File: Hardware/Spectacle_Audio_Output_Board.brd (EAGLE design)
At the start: 25.4 x 55.9 mm, 77 parts, among them J3 Audio Jack, J4 AUDIO-JACK3, J5 AUDIO-JACK3, U1 CY8C4146LQI-S422, U2 3.3V, U3 3.3V, U4 AT25SF041-SOIC8, Y1 12MHz

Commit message: Submitted for review by QC
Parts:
- added C11: 10uF, SparkFun-Capacitors:0603-CAP
- added FD5, FD6, FD7, FD8: FIDUCIALUFIDUCIAL, SparkFun-Aesthetics:MICRO-FIDUCIAL
- added R2: 1M, SparkFun-Resistors:0603-RES
- J3: value Audio Jack -> (none); device SparkFun-Connectors:STEREOJACK2.5MM_SMD -> SparkFun-Connectors:AUDIO-JACK-3.5MM-SMD
- moved C12 15.6 mm to (13.8, 27.8), turned to 90 degrees
- moved R20 7.80 mm to (19.2, 49.8), turned to 180 degrees
- moved R19 5.87 mm to (16.9, 40.4), turned to 180 degrees
- moved C13 5.08 mm to (19.2, 48.3)
- moved C15 5.08 mm to (19.2, 46.7)
- moved R21 5.08 mm to (22.9, 48.3)
- moved R24 5.08 mm to (22.9, 46.7)
- moved R22 3.07 mm to (20.6, 41.9)
- moved R23 3.07 mm to (20.6, 43.4)
- moved C14 3.07 mm to (16.9, 41.9)
- moved C16 3.07 mm to (16.9, 43.4)
- moved J3 2.54 mm to (0.00, 45.7)
- moved SW2 1.27 mm to (20.3, 34.3)
- moved U4 0.81 mm to (19.6, 29.8)
- moved C19 0.13 mm to (20.7, 18.2)
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- renumbered U$2 to U5
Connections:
- new net VCCIO: C12.1, R11.2, R12.2, R13.2, R14.2, R15.2, R16.2, R17.2, R29.2, U5.19, U5.30, U5.7
- new net VDDA: C11.1, U5.34, U5.39, U5.44, U5.46
- net 3.3V: now also C21.2; no longer C12.1, R11.2, R12.2, R13.2, R14.2, R15.2, R16.2, R17.2, R26.1, R29.2, U5.19, U5.30, U5.34, U5.39, U5.44, U5.46, U5.7
- net GND: now also C11.2, J3.SLEEVE, R2.2, R26.2; no longer C21.1, J3.5
- net L_AC: now also J3.TIP; no longer J3.1
- net N$12: now also R2.1
- net N$15: now also C21.1, R26.1; no longer C21.2, R26.2
- net R_AC: now also J3.RING; no longer J3.4
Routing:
- net VCCIO: track 0.00 -> 92.4 mm, vias 0 -> 10
- net 3.3V: track 65.3 -> 31.0 mm, vias 19 -> 9
- net R_AC: track 4.83 -> 31.6 mm
- net VDDA: track 0.00 -> 17.3 mm
- net L_AC: track 4.83 -> 13.7 mm
- net N$12: track 2.85 -> 11.2 mm, vias 0 -> 2
- net LEFT: track 47.3 -> 52.1 mm
- net VDD: track 23.7 -> 27.4 mm
- net N$7: track 21.6 -> 24.6 mm
- net RIGHT: track 40.7 -> 38.1 mm
- net N$1: track 26.0 -> 28.4 mm
- net SDCK: track 29.4 -> 31.2 mm
- net SCLK: track 8.19 -> 6.74 mm
- net SO: track 9.21 -> 7.92 mm
- net BTN: track 1.90 -> 3.17 mm
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
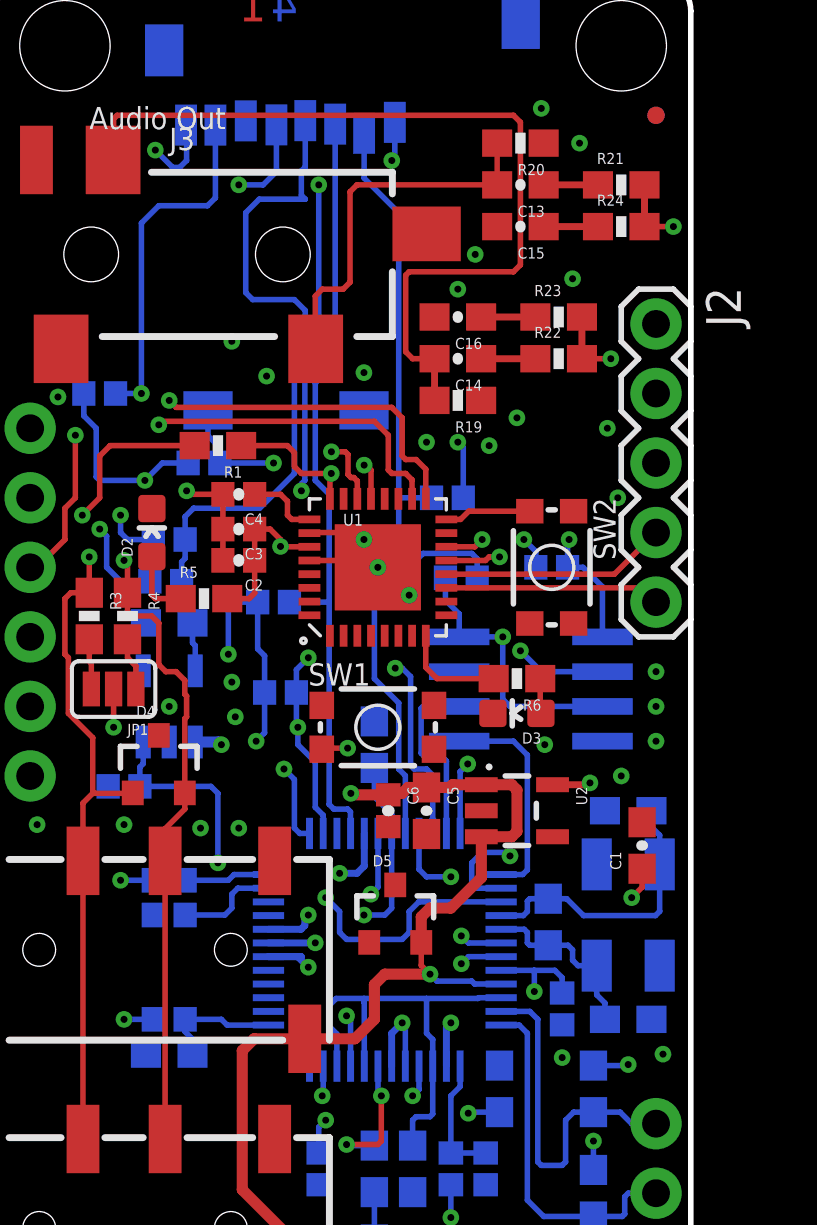
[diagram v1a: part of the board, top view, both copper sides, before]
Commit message: Fixes from QC review
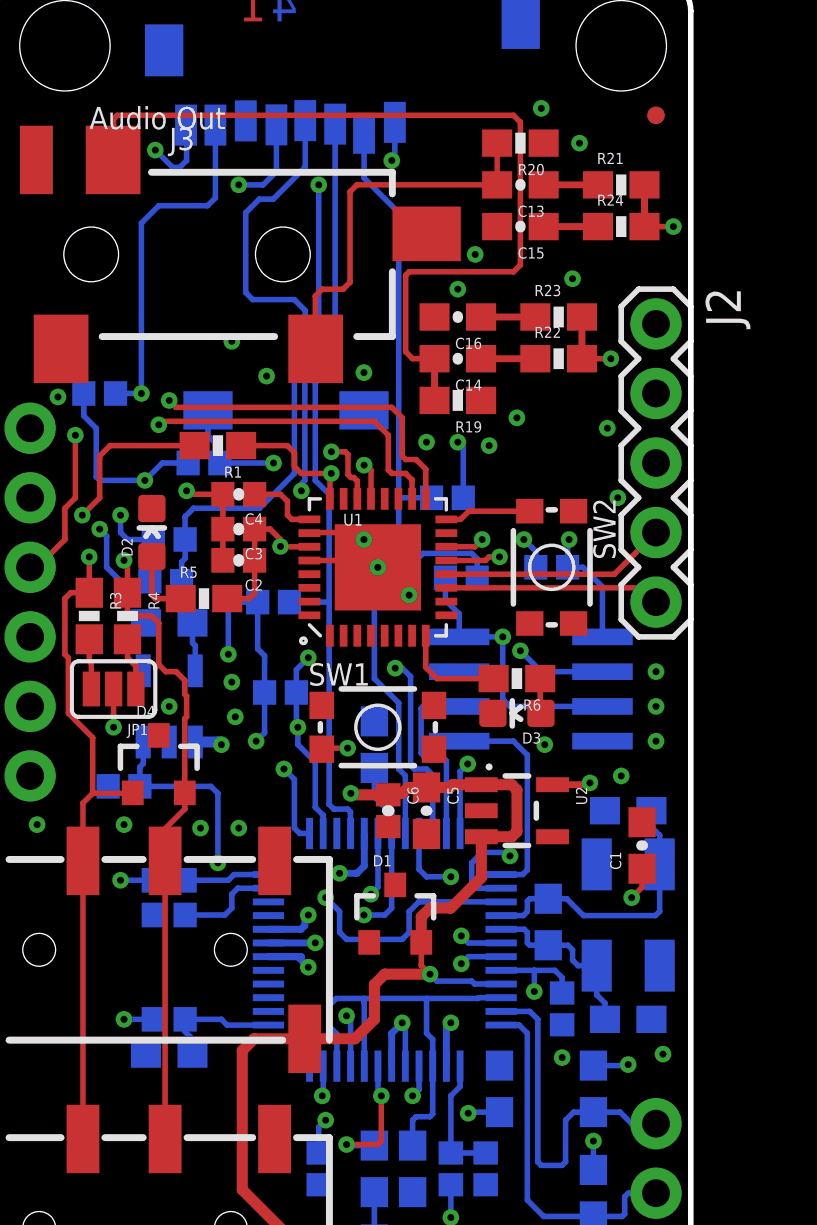
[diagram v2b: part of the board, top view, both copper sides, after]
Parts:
- renumbered C22 to C20, D5 to D1
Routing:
- net N$1: track 28.4 -> 27.0 mm
- net VDD: track 27.4 -> 26.6 mm
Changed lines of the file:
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@@
 <layers>
 <layer number="1" name="Top" color="4" fill="1" visible="no" active="yes"/>
-<layer number="2" name="Route2" color="1" fill="3" visible="no" active="yes"/>
+<layer number="2" name="Route2" color="1" fill="3" visible="yes" active="yes"/>
 <layer number="15" name="Route15" color="4" fill="6" visible="no" active="yes"/>
-<layer number="16" name="Bottom" color="1" fill="1" visible="yes" active="yes"/>
+<layer number="16" name="Bottom" color="1" fill="1" visible="no" active="yes"/>
 <layer number="17" name="Pads" color="2" fill="1" visible="yes" active="yes"/>
 <layer number="18" name="Vias" color="2" fill="1" visible="yes" active="yes"/>
@@
 <layer number="20" name="Dimension" color="15" fill="1" visible="yes" active="yes"/>
 <layer number="21" name="tPlace" color="16" fill="1" visible="no" active="yes"/>
-<layer number="22" name="bPlace" color="14" fill="1" visible="yes" active="yes"/>
+<layer number="22" name="bPlace" color="14" fill="1" visible="no" active="yes"/>
 <layer number="23" name="tOrigins" color="15" fill="1" visible="no" active="yes"/>
-<layer number="24" name="bOrigins" color="15" fill="1" visible="yes" active="yes"/>
+<layer number="24" name="bOrigins" color="15" fill="1" visible="no" active="yes"/>
 <layer number="25" name="tNames" color="7" fill="1" visible="no" active="yes"/>
 <layer number="26" name="bNames" color="7" fill="1" visible="no" active="yes"/>
@@
 <attribute name="PROD_ID" value="DIO-12501" x="5.969" y="27.051" size="1.778" layer="27" font="vector" ratio="15" display="off"/>
 </element>
-<element name="D5" library="SparkFun-DiscreteSemi" package="SOT23-3" value="PESD1CAN" x="14.605" y="21.59">
+<element name="D1" library="SparkFun-DiscreteSemi" package="SOT23-3" value="PESD1CAN" x="14.605" y="21.59">
 <attribute name="PROD_ID" value="DIO-12501" x="14.605" y="21.59" size="1.778" layer="27" font="vector" ratio="15" display="off"/>
 </element>
@@
 <attribute name="PROD_ID" value="RES-13495" x="20.32" y="34.29" size="1.778" layer="28" font="vector" ratio="15" rot="MR0" display="off"/>
 </element>
-<element name="C22" library="SparkFun-Capacitors" package="0603-CAP" value="2.2uF" x="6.35" y="32.258" rot="MR0">
+<element name="C20" library="SparkFun-Capacitors" package="0603-CAP" value="2.2uF" x="6.35" y="32.258" rot="MR0">
 <attribute name="PROD_ID" value="CAP-07888" x="6.35" y="32.258" size="1.778" layer="28" font="vector" ratio="15" rot="MR0" display="off"/>
 </element>
@@
 <contactref element="J4" pad="TIP"/>
 <contactref element="D4" pad="3"/>
-<contactref element="D5" pad="3"/>
+<contactref element="D1" pad="3"/>
 <polygon width="0.2032" layer="1" isolate="0.3048" rank="2">
 <vertex x="0" y="1.27"/>
@@
 <contactref element="U3" pad="2"/>
 <contactref element="U4" pad="4"/>
-<contactref element="C22" pad="2"/>
+<contactref element="C20" pad="2"/>
 <via x="16.637" y="17.653" extent="1-16" drill="0.254"/>
 <via x="14.859" y="17.653" extent="1-16" drill="0.254"/>
@@
 <wire x1="13.974" y1="22.61" x2="13.716" y2="22.352" width="0.2032" layer="16"/>
 <via x="13.716" y="22.352" extent="1-16" drill="0.254"/>
-<wire x1="20.574" y1="16.51" x2="20.701" y2="16.383" width="0.2032" layer="16"/>
 <via x="20.701" y="16.383" extent="1-16" drill="0.254"/>
 <via x="22.86" y="26.67" extent="1-16" drill="0.254"/>
@@
 <contactref element="C5" pad="1"/>
 <contactref element="J4" pad="EARTH"/>
-<contactref element="D5" pad="2"/>
+<contactref element="D1" pad="2"/>
 <contactref element="U3" pad="1"/>
 <contactref element="U5" pad="33"/>
@@
 <contactref element="R7" pad="2"/>
 <contactref element="JP2" pad="4"/>
-<contactref element="C22" pad="1"/>
+<contactref element="C20" pad="1"/>
 <wire x1="7.3" y1="30.5101" x2="7.3" y2="31.435" width="0.2032" layer="16"/>
 <wire x1="7.3" y1="31.435" x2="7.2" y2="31.535" width="0.2032" layer="16"/>
@@
 <wire x1="6.93" y1="34.616" x2="6.93" y2="35.306" width="0.2032" layer="16"/>
 <wire x1="11.318425" y1="50.606296875" x2="11.318425" y2="48.910425" width="0.2032" layer="16"/>
-<wire x1="11.318425" y1="48.910425" x2="11.176" y2="48.768" width="0.2032" layer="16"/>
-<wire x1="11.176" y1="48.768" x2="11.176" y2="47.879" width="0.2032" layer="16"/>
-<wire x1="11.176" y1="47.879" x2="11.318425" y2="47.736575" width="0.2032" layer="16"/>
 <wire x1="11.318425" y1="41.925425" x2="10.922" y2="41.529" width="0.2032" layer="16"/>
 <wire x1="10.922" y1="41.529" x2="10.922" y2="37.719" width="0.2032" layer="16"/>
@@
 <wire x1="9.144" y1="44.323" x2="9.144" y2="47.244" width="0.2032" layer="16"/>
 <wire x1="9.144" y1="47.244" x2="9.636575" y2="47.736575" width="0.2032" layer="16"/>
-<wire x1="9.636575" y1="47.736575" x2="11.318425" y2="47.736575" width="0.2032" layer="16"/>
 <wire x1="11.318425" y1="41.925425" x2="11.318425" y2="43.672575" width="0.2032" layer="16"/>
+<wire x1="9.636575" y1="47.736575" x2="10.144575" y2="47.736575" width="0.2032" layer="16"/>
+<wire x1="10.144575" y1="47.736575" x2="11.318425" y2="48.910425" width="0.2032" layer="16"/>
 </signal>
 <signal name="N$1">
@@
 <wire x1="14.605" y1="50.52741875" x2="14.589215625" y2="50.543203125" width="0.2032" layer="16"/>
 <wire x1="14.097" y1="48.768" x2="14.478" y2="49.149" width="0.2032" layer="2"/>
-<wire x1="14.478" y1="49.149" x2="14.478" y2="50.4319875" width="0.2032" layer="2"/>
-<wire x1="14.478" y1="50.4319875" x2="14.589215625" y2="50.543203125" width="0.2032" layer="2"/>
 <wire x1="14.589215625" y1="50.543203125" x2="14.589215625" y2="49.260215625" width="0.2032" layer="16"/>
 <wire x1="14.589215625" y1="49.260215625" x2="14.478" y2="49.149" width="0.2032" layer="16"/>

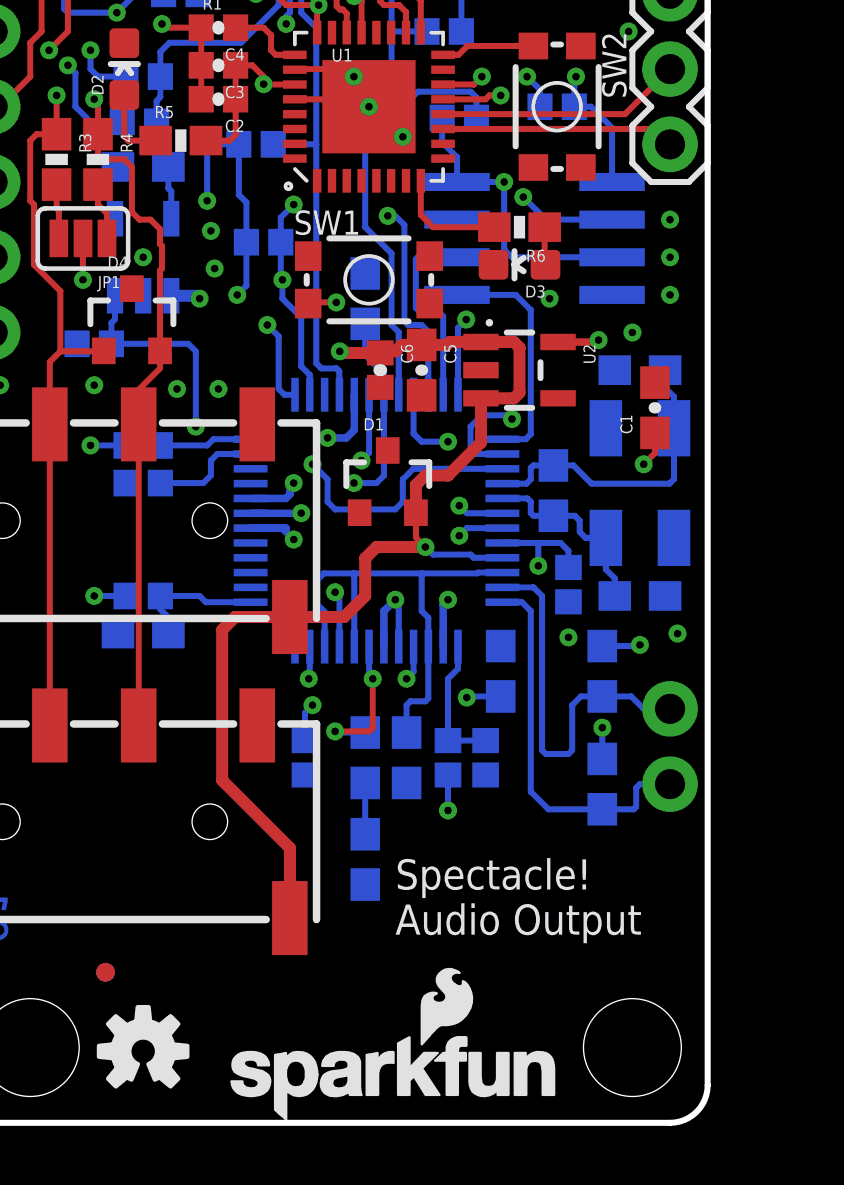
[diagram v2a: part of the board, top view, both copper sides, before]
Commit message: Added downstream power control circuitry
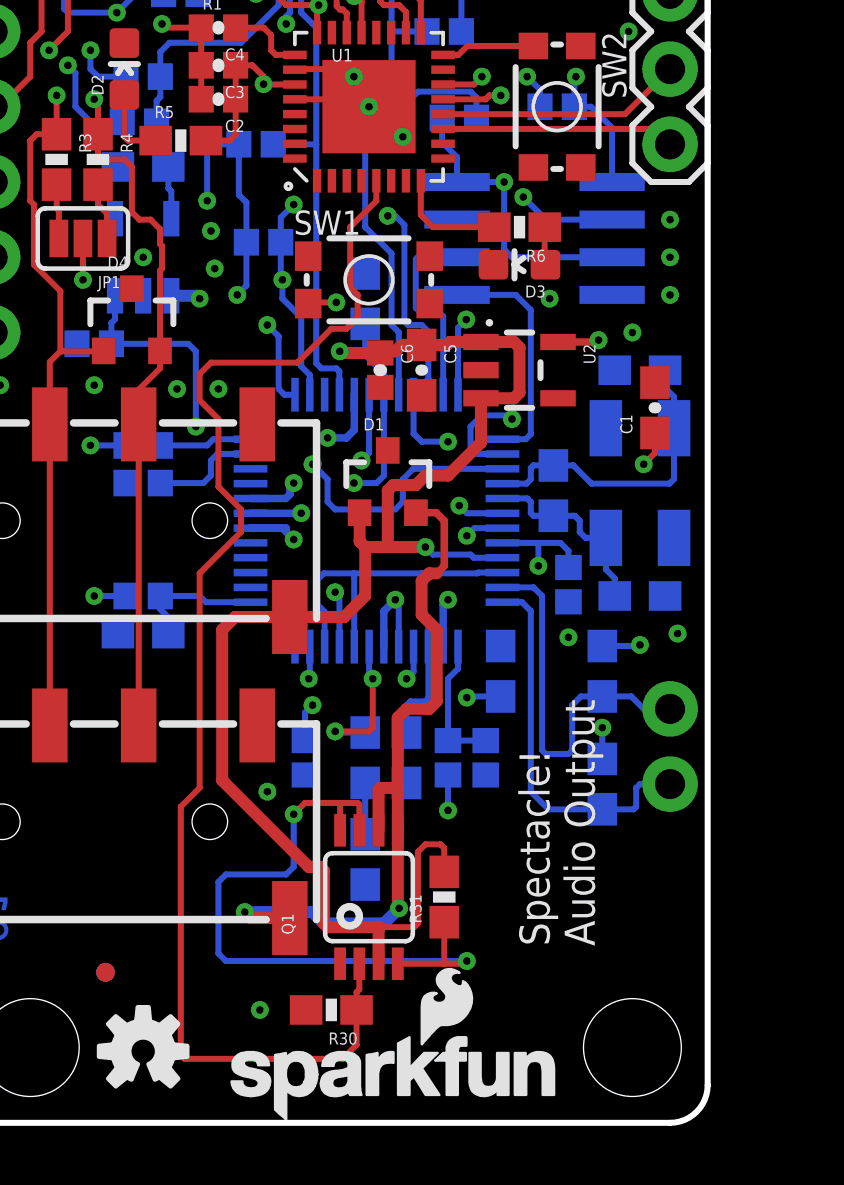
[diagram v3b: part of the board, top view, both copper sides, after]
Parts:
- added Q1: (no value), SparkFun-DiscreteSemi:MSOP8
- added R30, R31: 10K, SparkFun-Resistors:0603-RES
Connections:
- new net N$26: Q1.4, Q1.7, Q1.8, R31.1
- new net VOUT: D1.2, J5.EARTH, Q1.5, Q1.6
- new net V_OUT_EN: Q1.2, R30.1, U1.5
- net GND: now also Q1.1, R30.2
- net VIN: now also D1.1, Q1.3, R31.2; no longer D1.2, J5.EARTH
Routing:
- net V_OUT_EN: track 0.00 -> 44.6 mm
- net VOUT: track 0.00 -> 25.1 mm, vias 0 -> 2
- net N$26: track 0.00 -> 23.4 mm, vias 0 -> 2
- net VIN: track 45.3 -> 57.1 mm
- net GND: track 27.5 -> 27.2 mm, vias 36 -> 38
